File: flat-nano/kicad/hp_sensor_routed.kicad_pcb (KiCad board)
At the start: 4 copper layers, 99.9 x 17.8 mm, 72 parts, among them J1 Hand-soldered cable (3 wires), J2 programming clip holes, J5 recovery clip holes (SWD), Q1 AO3400A, Q2 AO3400A, U1 R7FA4M1AB3CFM, U3 HT7550-1, U4 INA226, Y1 32.768kHz 12.5pF 3215

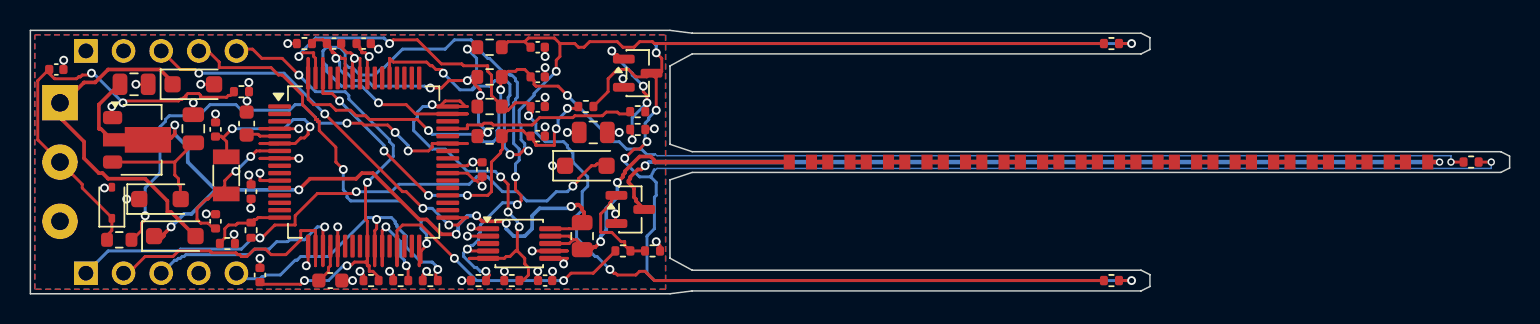
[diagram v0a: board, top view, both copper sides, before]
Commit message: Update flat-nano and hat to the reviewed designs; refresh the website
Boards (both at the Arduino Nano R4 outline, 43.18 x 17.78 mm):
- Hand-routed copper (preroute.py) replaces the auto-router; release.py
  rebuilds, checks (ERC, DRC all severities, parity, Kelvin, solder vias,
  layout quality) and exports the order files with a release manifest.
- Layout quality gate: power copper >= 0.5 mm outer / 1.2 mm inner,
  heat sources on the center line, mirrored side needles, left/right
  copper within 10% on every layer.
- flat-nano: 5 V buck regulator (LMR36503), single-sided assembly,
  cable solder holes, programming-clip holes. Hat: parts on both faces,
  Nano pins kept.
- R11 330 ohm -> 1.5 kohm so pin D4 stays within the RA4M1 4 mA limit.
- TH1 is the right needle and TH3 the left, as seen on the top face with
  the cable end up (pin map unchanged: A2 = TH1, A0 = TH3).
- No revision labels; old-version checksums and auto-router reports
  removed.

Website (docs/) and twin:
- Board data, drawing, current-flow lines, tags, parts list, guided tour
  and model match the current flat-nano.
- Plainer wording for the C3/C4 filtering explanations.

Co-Authored-By: Claude Opus 5.5 <noreply@anthropic.com>
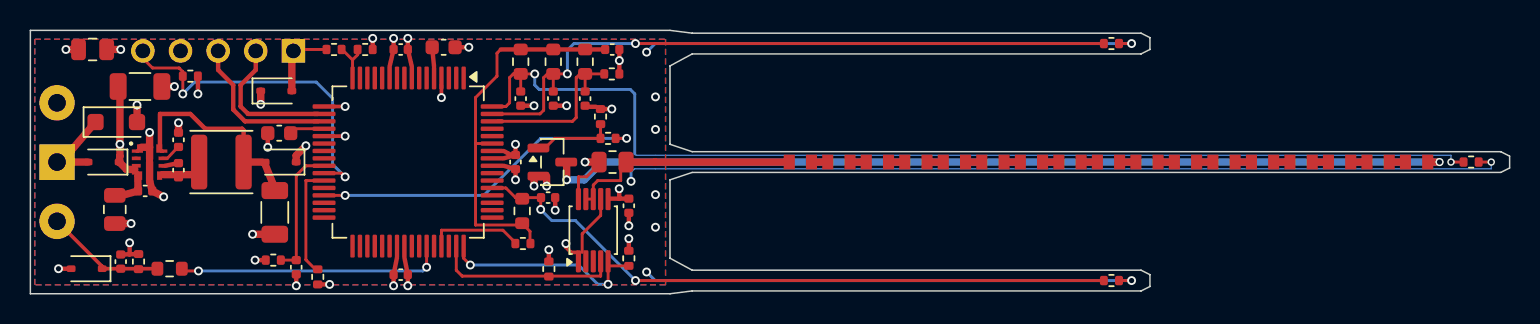
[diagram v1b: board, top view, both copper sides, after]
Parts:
- removed C5, C6: 18p, C_0402_1005Metric
- removed J5: recovery clip holes (SWD), ClipRow_1x05_P2.54mm
- removed Q2: AO3400A, SOT-23
- removed R12: 1.5k, R_0402_1005Metric
- removed R17: 100k, R_0402_1005Metric
- removed Y1: 32.768kHz 12.5pF 3215, Crystal_SMD_3215-2Pin_3.2x1.5mm
- added C18: 100n 50V, C_0402_1005Metric, F.Cu at (107.8, 82.0)
- added C19: 100n, C_0402_1005Metric, F.Cu at (110.0, 80.5)
- added C20: 1u, C_0402_1005Metric, F.Cu at (110.0, 78.5)
- added C3: 22u 25V, C_1206_3216Metric, F.Cu at (107.4, 74.9)
- added L1: 22uH, L_Sunlord_SWPA4020S, F.Cu at (112.9, 80.0)
- C17: value 10u 10V -> 10u 25V
- C2: value 10u 10V -> 22u 25V; footprint C_0805_2012Metric -> C_1206_3216Metric
- D1, D5, D7: value 1A 40V Schottky (SOD-123F) -> 1A 40V Schottky (SOD-323); footprint D_SOD-123F -> D_SOD-323
- R11: value 10 -> 1.5k
- U3: value HT7550-1 -> LMR36503R5RPER; footprint SOT-89-3 -> TI_RPE0009A_VQFN-HR-9_2x2mm
- moved C17 34.3 mm to (104.2, 72.4)
- moved D5 21.5 mm to (116.6, 75.2)
- moved R2 21.3 mm to (110.8, 74.2), turned to 180 degrees
- moved J2 20.5 mm to (117.8, 72.5), turned to 180 degrees
- moved R11 20.0 mm to (133.2, 85.5)
- moved C13 18.8 mm to (139.3, 72.4)
- moved R16 16.1 mm to (122.6, 72.4)
- moved C10 14.3 mm to (127.9, 72.2), turned to 0 degrees
- moved C7 13.9 mm to (125.0, 72.4), turned to 0 degrees
- moved C4 13.7 mm to (106.1, 86.7), turned to 90 degrees
- moved R15 13.4 mm to (120.5, 72.4), turned to 0 degrees
- moved R4 13.4 mm to (107.3, 86.7), turned to 90 degrees
- moved C9 13.0 mm to (132.8, 80.0), turned to 90 degrees
- moved C16 10.5 mm to (116.8, 78.0), turned to 180 degrees
- moved R10 9.73 mm to (138.5, 76.9), turned to 90 degrees
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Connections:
- C2 pad 1: 5V_LDO -> 5V_BUCK
- C21 pad 1: A0_TH1 -> A2_TH1
- C23 pad 1: A2_TH3 -> A0_TH3
- D7 pad 2: 5V_LDO -> 5V_BUCK
- R11 pad 1: +5V -> D4_EXC
- R21 pad 2: A0_TH1 -> A2_TH1
- R23 pad 2: A2_TH3 -> A0_TH3
- TH1 pad 1: A0_TH1 -> A2_TH1
- TH1 pad 2: TH_RTN -> GND
- TH2 pad 2: TH_RTN -> GND
- TH3 pad 1: A2_TH3 -> A0_TH3
- TH3 pad 2: TH_RTN -> GND
- TH4 pad 2: TH_RTN -> GND
- U1 pad 32: SWCLK -> (no net)
- U1 pad 33: SWDIO -> (no net)
- U1 pad 53: A0_TH1 -> A0_TH3
- U1 pad 6: XCIN -> (no net)
- U1 pad 63: A2_TH3 -> A2_TH1
- U1 pad 7: XCOUT -> (no net)
- U3 pad 2: VIN_P -> (no net)
- U3 pad 3: 5V_LDO -> VIN_P
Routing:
- net TH_RTN: track 150.2 -> 0.00 mm, vias 7 -> 0
- net GND: track 36.6 -> 164.7 mm, vias 32 -> 37
- net A2_TH3: track 71.4 -> 0.00 mm, vias 4 -> 0
- net A0_TH1: track 68.3 -> 0.00 mm, vias 4 -> 0
- net A2_TH1: track 0.00 -> 45.3 mm, vias 0 -> 2
- net A0_TH3: track 0.00 -> 44.2 mm, vias 0 -> 2
- net A4_SDA: track 49.2 -> 11.4 mm, vias 5 -> 0
- net VUSB: track 40.7 -> 3.73 mm, vias 3 -> 0
- net SWCLK: track 27.1 -> 0.00 mm, vias 2 -> 0
- net SWDIO: track 27.0 -> 0.00 mm, vias 4 -> 0
- net RESET: track 33.4 -> 8.50 mm, vias 4 -> 0
- net SDI_LINE: track 28.6 -> 7.06 mm, vias 2 -> 0
- net A3_TH4: track 30.3 -> 10.2 mm, vias 6 -> 0
- net VIN: track 23.6 -> 4.86 mm
- net A1_TH2: track 90.9 -> 72.9 mm, vias 4 -> 2
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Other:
- board text added: "5V D- D+ G B"
- board text added: "HP-NANO"
- board text removed: "5V"
- board text removed: "B"
- board text removed: "D+"
- board text removed: "D-"
- board text removed: "G"
- board text removed: "G 5V IO CK RS"
- board text removed: "HP-NANO r2"

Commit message: Prefer JLC Basic/Preferred parts and fewer BOM lines; wider primer page
Flat-nano 27 -> 25 BOM lines (13 -> 9 Extended), hat 21 -> 20 (10 -> 6):
- Schottky diodes: 1N5819WS C191023 (Basic, same SOD-323)
- C1 and C17: one 10 uF 50 V 0805 part, C440198 (Basic)
- all 100 nF: the 50 V part C307331 (Basic)
- C4 3.3 nF: C26404 (Preferred); SMF16CA/SMF15CA TVS: C19077511/C19077510 (Preferred)
Copper and placement unchanged (all tracks, vias and positions identical); full
release checks pass. Twin parts data, flat-nano README and primer Appendix A
updated to match.

Primer page: wider column, larger text and more space between sections on
screen; print layout unchanged.

Co-Authored-By: Claude Opus 5.5 <noreply@anthropic.com>
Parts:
- C1: value 4.7u 50V -> 10u 50V
- C17: value 10u 25V -> 10u 50V
- C18: value 100n 50V -> 100n
